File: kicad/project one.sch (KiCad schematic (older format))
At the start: 0 parts

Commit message: ..more work
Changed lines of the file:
@@
 $Descr USLetter 11000 8500
 encoding utf-8
-Sheet 1 4
+Sheet 1 6
 Title "Project One"
-Date "4 may 2014"
+Date "5 may 2014"
 Rev "0.0.0"
 Comp "Ali Kocaturk"
@@
 $EndSheet
 $Sheet
-S 3950 3100 2000 1250
+S 4200 2950 2000 1250
 U 5365F364
 F0 "MPU" 50
 F1 "project one mpu.sch" 50
+F2 "TWIMS0" B L 4200 3700 60
+F3 "IISC" B L 4200 3550 60
+F4 "ADC_OVF" I L 4200 3250 60
+F5 "AUDIO_RESET" O L 4200 3100 60
+F6 "DAC_XSMT" O R 6200 3050 60
+F7 "DAC_FLT" O R 6200 3200 60
 $EndSheet
 $Sheet
-S 1050 2500 1400 1100
+S 1400 3000 1400 1100
 U 536732E3
 F0 "ADC" 50
 F1 "project one adc.sch" 50
+F2 "IISC" B R 2800 3550 60
+F3 "TWIMS0" B R 2800 3700 60
+F4 "~RESET" I R 2800 3100 60
+F5 "OVER" O R 2800 3250 60
+$EndSheet
+Wire Bus Line
+	2800 3550 4200 3550
+Wire Bus Line
+	2800 3700 4200 3700
+Text Label 3800 3550 0    60   ~ 0
+IISC
+Text Label 3800 3700 0    60   ~ 0
+TWIMS0
+Wire Wire Line
+	4200 3100 2800 3100
+Wire Wire Line
+	4200 3250 2800 3250
+$Sheet
+S 7100 2950 1750 1250
+U 53675CA8
+F0 "DAC" 50
+F1 "project one dac.sch" 50
+F2 "OUTL" O L 7100 4050 60
+F3 "OUTR" O L 7100 4150 60
+F4 "FLT" I L 7100 3200 60
+F5 "XSMT" I L 7100 3050 60
+F6 "IISC" B L 7100 3550 60
+$EndSheet
+Wire Bus Line
+	3650 3550 3650 4500
+Wire Bus Line
+	3650 4500 6700 4500
+Wire Bus Line
+	6700 4500 6700 3550
+Wire Bus Line
+	6700 3550 7100 3550
+Wire Wire Line
+	6200 3050 7100 3050
+Wire Wire Line
+	6200 3200 7100 3200
+$Sheet
+S 7100 4850 1750 1450
+U 5367165F
+F0 "Amplifier" 50
+F1 "project one amplifier.sch" 50
 $EndSheet
 $EndSCHEMATC

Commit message: Version 0.0.0
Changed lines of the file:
@@
 Sheet 1 6
 Title "Project One"
-Date "5 may 2014"
+Date "6 may 2014"
 Rev "0.0.0"
 Comp "Ali Kocaturk"
@@
 	3650 4500 6700 4500
 Wire Bus Line
-	6700 4500 6700 3550
+	6700 3550 6700 5400
 Wire Bus Line
 	6700 3550 7100 3550
@@
 F0 "Amplifier" 50
 F1 "project one amplifier.sch" 50
+F2 "HP_DETECT" O L 7100 6200 60
+F3 "SPK_FAULT" O L 7100 6100 60
+F4 "SPK_SD" I L 7100 6000 60
+F5 "TWIMS0" B L 7100 5550 60
+F6 "IISC" B L 7100 5400 60
+F7 "DR_MUTE" I L 7100 5900 60
+F8 "HP_IN L" I L 7100 4950 60
+F9 "HP_IN R" I L 7100 5050 60
 $EndSheet
+Wire Wire Line
+	7100 4950 7000 4950
+Wire Wire Line
+	7000 4950 7000 4050
+Wire Wire Line
+	7000 4050 7100 4050
+Wire Wire Line
+	7100 4150 6900 4150
+Wire Wire Line
+	6900 4150 6900 5050
+Wire Wire Line
+	6900 5050 7100 5050
+Wire Bus Line
+	6700 5400 7100 5400
+Wire Bus Line
+	7100 5550 3500 5550
+Wire Bus Line
+	3500 5550 3500 3700
 $EndSCHEMATC

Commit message: More stuff....
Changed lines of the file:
@@
 Sheet 1 6
 Title "Project One"
-Date "6 may 2014"
+Date "9 may 2014"
 Rev "0.0.0"
 Comp "Ali Kocaturk"
@@
 $EndSheet
 $Sheet
+S 1400 3000 1400 1100
+U 536732E3
+F0 "ADC" 50
+F1 "project one adc.sch" 50
+F2 "IISC" B R 2800 3550 60
+F3 "TWIMS0" B R 2800 3700 60
+F4 "~RESET" I R 2800 3100 60
+F5 "OVER" O R 2800 3250 60
+$EndSheet
+Text Label 3800 3550 0    60   ~ 0
+IISC
+Text Label 3800 3700 0    60   ~ 0
+TWIMS0
+$Sheet
+S 7400 2950 1750 1250
+U 53675CA8
+F0 "DAC" 50
+F1 "project one dac.sch" 50
+F2 "OUTL" O L 7400 4050 60
+F3 "OUTR" O L 7400 4150 60
+F4 "FLT" I L 7400 3200 60
+F5 "XSMT" I L 7400 3050 60
+F6 "IISC" B L 7400 3550 60
+$EndSheet
+$Sheet
+S 7400 4850 1750 1450
+U 5367165F
+F0 "Amplifier" 50
+F1 "project one amplifier.sch" 50
+F2 "HP_DETECT" O L 7400 6200 60
+F3 "SPK_FAULT" O L 7400 6100 60
+F4 "SPK_SD" I L 7400 6000 60
+F5 "TWIMS0" B L 7400 5550 60
+F6 "IISC" B L 7400 5400 60
+F7 "DR_MUTE" I L 7400 5900 60
+F8 "HP_IN L" I L 7400 4950 60
+F9 "HP_IN R" I L 7400 5050 60
+$EndSheet
+$Sheet
 S 4200 2950 2000 1250
 U 5365F364
@@
 F6 "DAC_XSMT" O R 6200 3050 60
 F7 "DAC_FLT" O R 6200 3200 60
-$EndSheet
-$Sheet
-S 1400 3000 1400 1100
-U 536732E3
-F0 "ADC" 50
-F1 "project one adc.sch" 50
-F2 "IISC" B R 2800 3550 60
-F3 "TWIMS0" B R 2800 3700 60
-F4 "~RESET" I R 2800 3100 60
-F5 "OVER" O R 2800 3250 60
+F8 "AMP_SPK_FAULT" I R 6200 4000 60
+F9 "AMP_SPK_SD" O R 6200 3900 60
+F10 "AMP_DR_MUTE" O R 6200 3800 60
+F11 "AMP_HP_DETECT" I R 6200 4100 60
 $EndSheet
 Wire Bus Line
@@
 Wire Bus Line
 	2800 3700 4200 3700
-Text Label 3800 3550 0    60   ~ 0
-IISC
-Text Label 3800 3700 0    60   ~ 0
-TWIMS0
 Wire Wire Line
 	4200 3100 2800 3100
 Wire Wire Line
 	4200 3250 2800 3250
-$Sheet
-S 7100 2950 1750 1250
-U 53675CA8
-F0 "DAC" 50
-F1 "project one dac.sch" 50
-F2 "OUTL" O L 7100 4050 60
-F3 "OUTR" O L 7100 4150 60
-F4 "FLT" I L 7100 3200 60
-F5 "XSMT" I L 7100 3050 60
-F6 "IISC" B L 7100 3550 60
-$EndSheet
 Wire Bus Line
 	3650 3550 3650 4500
 Wire Bus Line
-	3650 4500 6700 4500
+	3650 4500 7000 4500
 Wire Bus Line
-	6700 3550 6700 5400
+	7000 3550 7000 5400
 Wire Bus Line
-	6700 3550 7100 3550
+	7000 3550 7400 3550
 Wire Wire Line
-	6200 3050 7100 3050
+	6200 3050 7400 3050
 Wire Wire Line
-	6200 3200 7100 3200
-$Sheet
-S 7100 4850 1750 1450
-U 5367165F
-F0 "Amplifier" 50
-F1 "project one amplifier.sch" 50
-F2 "HP_DETECT" O L 7100 6200 60
-F3 "SPK_FAULT" O L 7100 6100 60
-F4 "SPK_SD" I L 7100 6000 60
-F5 "TWIMS0" B L 7100 5550 60
-F6 "IISC" B L 7100 5400 60
-F7 "DR_MUTE" I L 7100 5900 60
-F8 "HP_IN L" I L 7100 4950 60
-F9 "HP_IN R" I L 7100 5050 60
-$EndSheet
+	6200 3200 7400 3200
 Wire Wire Line
-	7100 4950 7000 4950
+	7400 4950 7300 4950
 Wire Wire Line
-	7000 4950 7000 4050
+	7300 4950 7300 4050
 Wire Wire Line
-	7000 4050 7100 4050
+	7300 4050 7400 4050
 Wire Wire Line
-	7100 4150 6900 4150
+	7400 4150 7200 4150
 Wire Wire Line
-	6900 4150 6900 5050
+	7200 4150 7200 5050
 Wire Wire Line
-	6900 5050 7100 5050
+	7200 5050 7400 5050
 Wire Bus Line
-	6700 5400 7100 5400
+	7000 5400 7400 5400
 Wire Bus Line
-	7100 5550 3500 5550
+	7400 5550 3500 5550
 Wire Bus Line
 	3500 5550 3500 3700
+Wire Wire Line
+	6200 4100 6300 4100
+Wire Wire Line
+	6300 4100 6300 6200
+Wire Wire Line
+	6300 6200 7400 6200
+Wire Wire Line
+	7400 6100 6400 6100
+Wire Wire Line
+	6400 6100 6400 4000
+Wire Wire Line
+	6400 4000 6200 4000
+Wire Wire Line
+	6200 3900 6500 3900
+Wire Wire Line
+	6500 3900 6500 6000
+Wire Wire Line
+	6500 6000 7400 6000
+Wire Wire Line
+	7400 5900 6600 5900
+Wire Wire Line
+	6600 5900 6600 3800
+Wire Wire Line
+	6600 3800 6200 3800
 $EndSCHEMATC

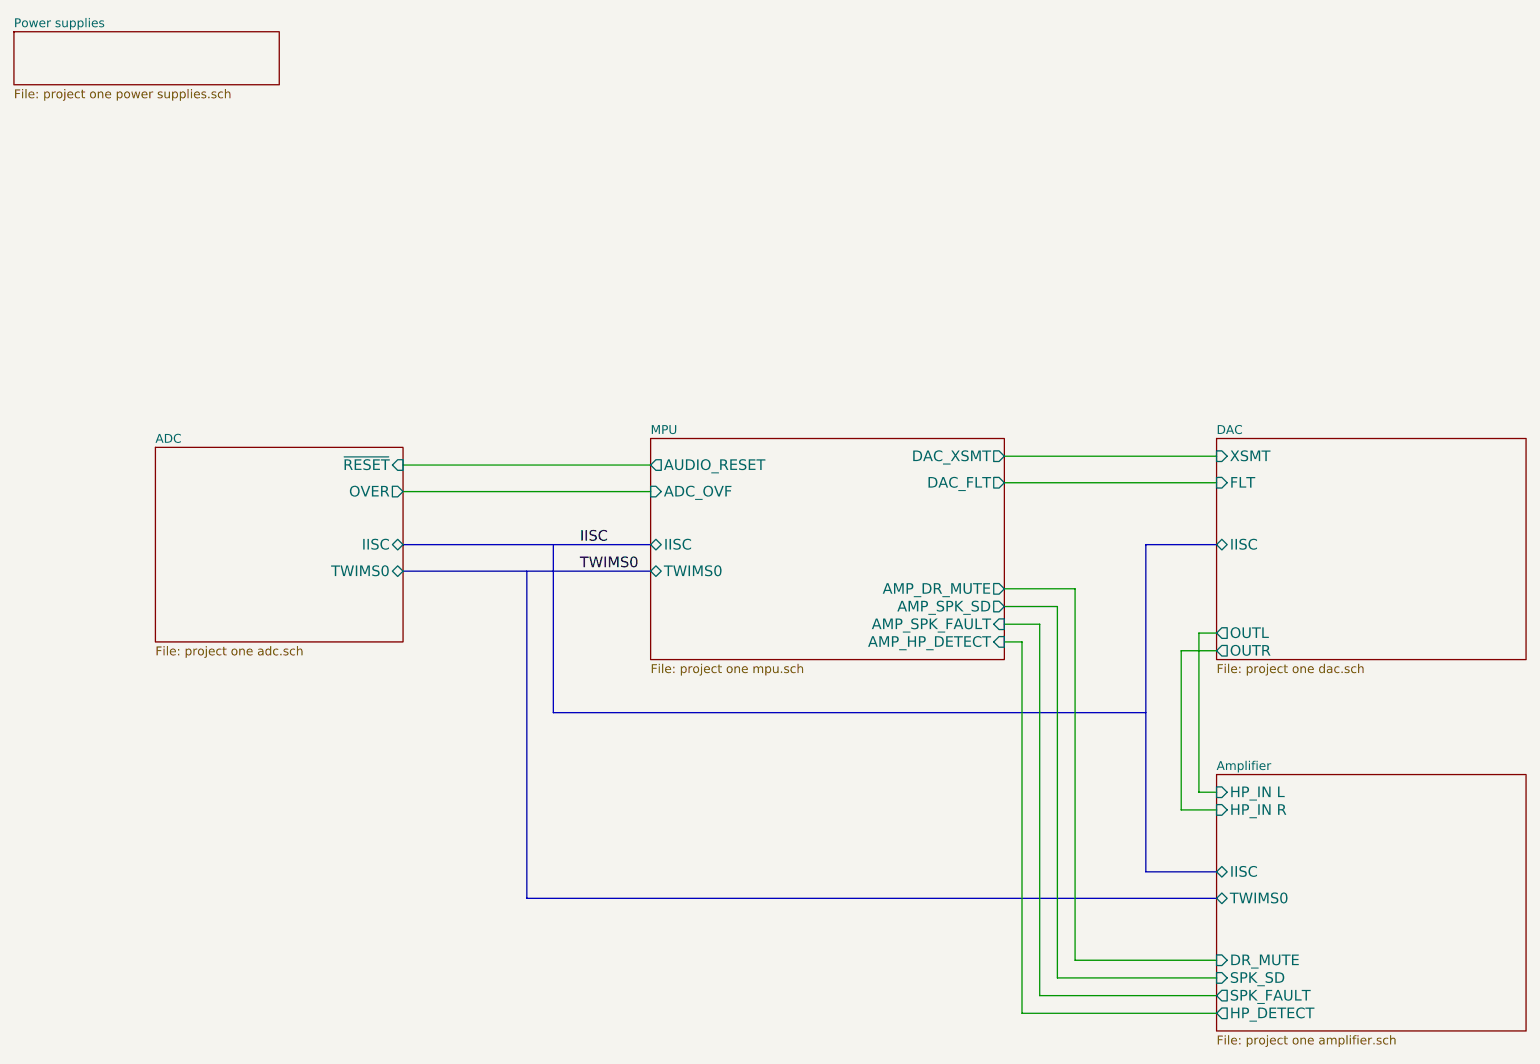
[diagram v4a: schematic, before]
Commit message: Begin switch to analog power amp
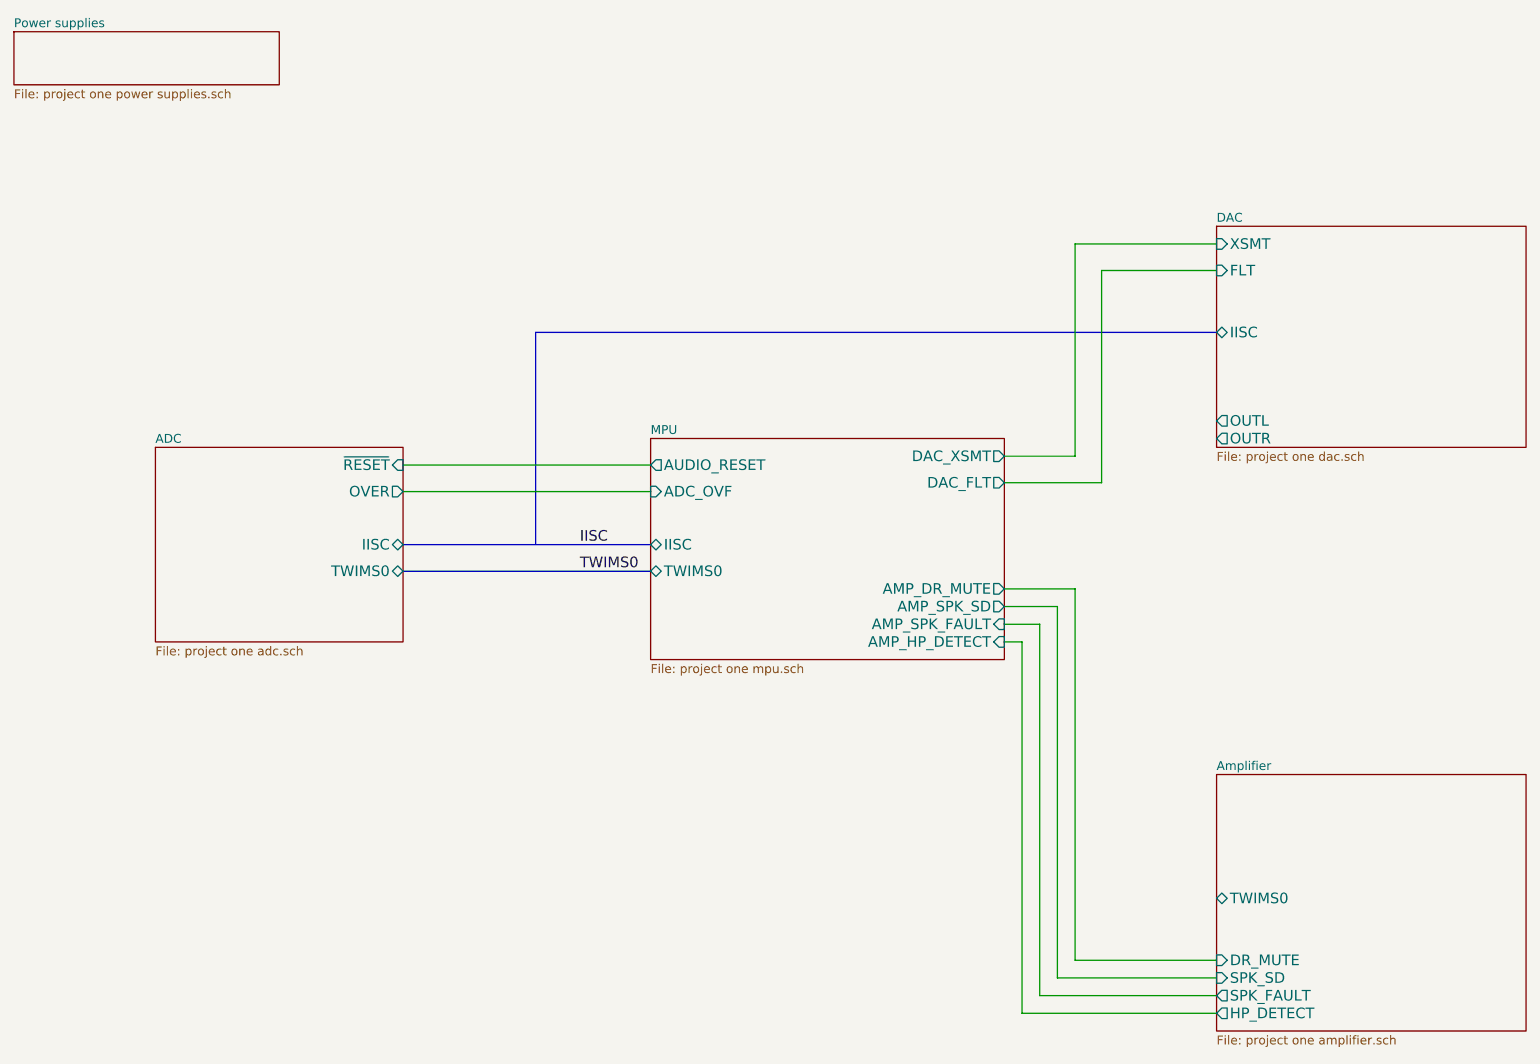
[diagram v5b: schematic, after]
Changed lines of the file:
@@
 Sheet 1 6
 Title "Project One"
-Date "27 may 2014"
+Date "18 jun 2014"
 Rev "0.0.0"
 Comp "Ali Kocaturk"
@@
 TWIMS0
 $Sheet
-S 7400 2950 1750 1250
+S 7400 1750 1750 1250
 U 53675CA8
 F0 "DAC" 50
 F1 "project one dac.sch" 50
-F2 "OUTL" O L 7400 4050 60
-F3 "OUTR" O L 7400 4150 60
-F4 "FLT" I L 7400 3200 60
-F5 "XSMT" I L 7400 3050 60
-F6 "IISC" B L 7400 3550 60
+F2 "OUTL" O L 7400 2850 60
+F3 "OUTR" O L 7400 2950 60
+F4 "FLT" I L 7400 2000 60
+F5 "XSMT" I L 7400 1850 60
+F6 "IISC" B L 7400 2350 60
 $EndSheet
 $Sheet
@@
 F4 "SPK_SD" I L 7400 6000 60
 F5 "TWIMS0" B L 7400 5550 60
-F6 "IISC" B L 7400 5400 60
-F7 "DR_MUTE" I L 7400 5900 60
-F8 "HP_IN L" I L 7400 4950 60
-F9 "HP_IN R" I L 7400 5050 60
+F6 "DR_MUTE" I L 7400 5900 60
 $EndSheet
 $Sheet
@@
 Wire Wire Line
 	4200 3250 2800 3250
-Wire Bus Line
-	3650 3550 3650 4500
-Wire Bus Line
-	3650 4500 7000 4500
-Wire Bus Line
-	7000 3550 7000 5400
-Wire Bus Line
-	7000 3550 7400 3550
-Wire Wire Line
-	6200 3050 7400 3050
-Wire Wire Line
-	6200 3200 7400 3200
-Wire Wire Line
-	7400 4950 7300 4950
-Wire Wire Line
-	7300 4950 7300 4050
-Wire Wire Line
-	7300 4050 7400 4050
-Wire Wire Line
-	7400 4150 7200 4150
-Wire Wire Line
-	7200 4150 7200 5050
-Wire Wire Line
-	7200 5050 7400 5050
-Wire Bus Line
-	7000 5400 7400 5400
-Wire Bus Line
-	7400 5550 3500 5550
-Wire Bus Line
-	3500 5550 3500 3700
 Wire Wire Line
 	6200 4100 6300 4100
@@
 Wire Wire Line
 	6600 3800 6200 3800
+Wire Wire Line
+	6200 3200 6750 3200
+Wire Wire Line
+	6750 3200 6750 2000
+Wire Wire Line
+	6750 2000 7400 2000
+Wire Wire Line
+	7400 1850 6600 1850
+Wire Wire Line
+	6600 1850 6600 3050
+Wire Wire Line
+	6600 3050 6200 3050
+Wire Bus Line
+	3550 3550 3550 2350
+Wire Bus Line
+	3550 2350 7400 2350
 $EndSCHEMATC
